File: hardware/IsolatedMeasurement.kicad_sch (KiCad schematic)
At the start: 25 parts, among them IC12 UCC12040DVE, IC15 ISO6763FDWR, IC2 MCP3561T-E_NC, IC5 SN74LVC1G07DBVR, IC6 AP7365-33YRG-13, IC9 REF193GSZ-REEL, J4 M300-MV10345M1

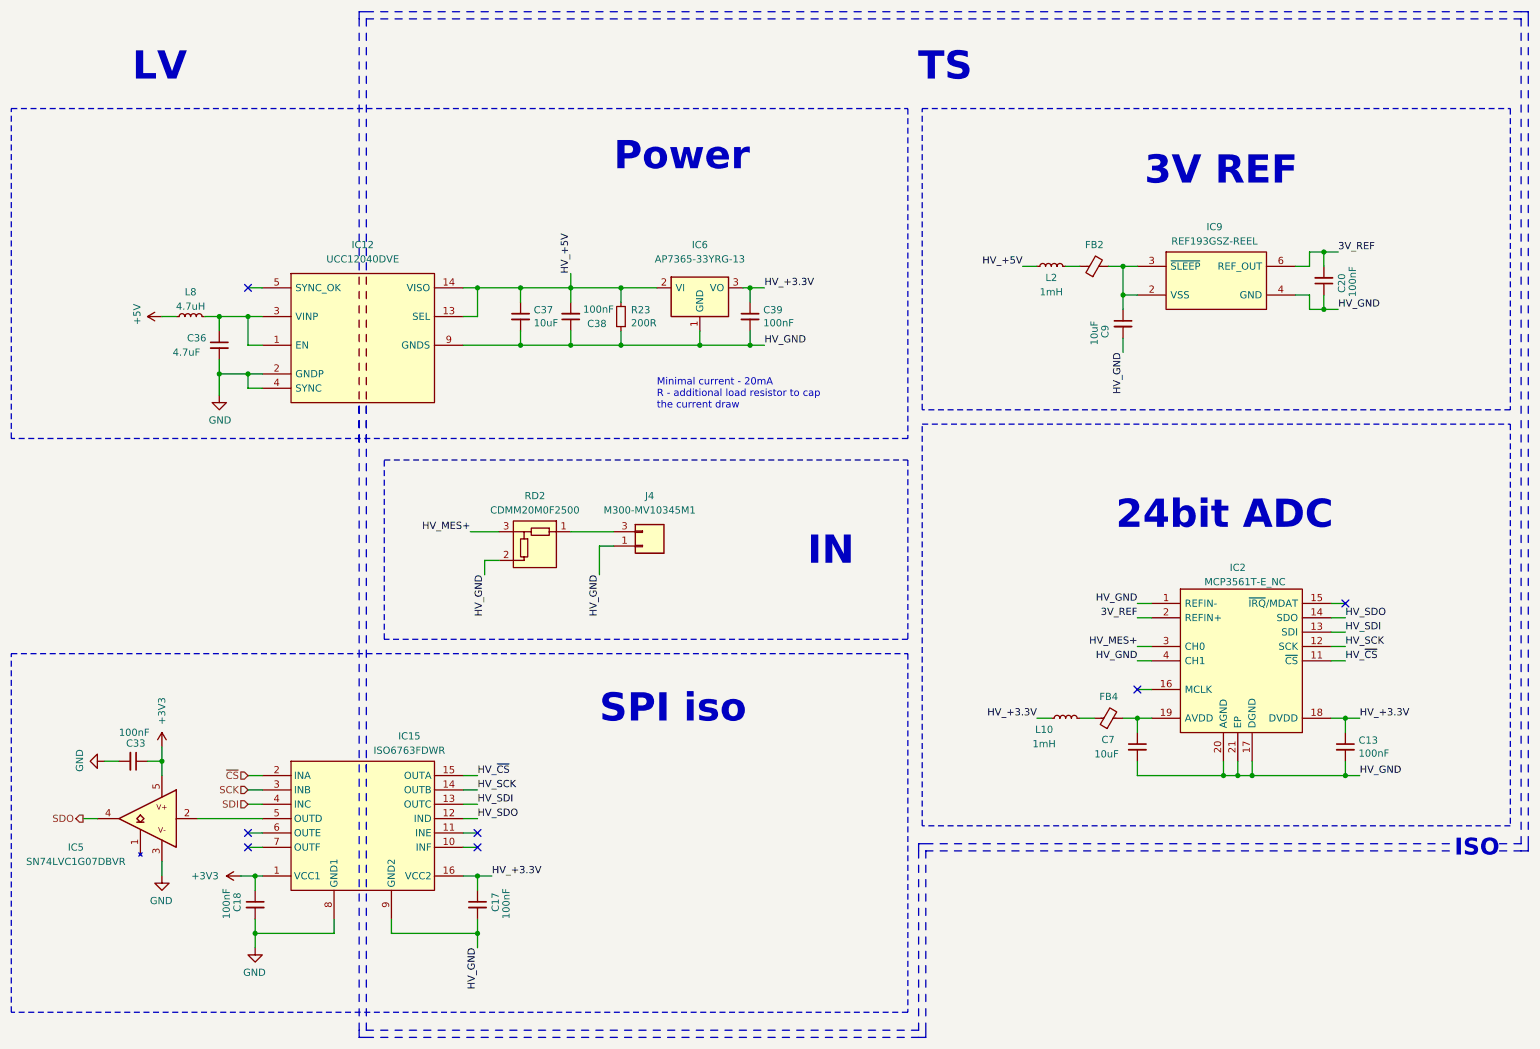
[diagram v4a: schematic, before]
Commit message: relay new driving logic, some ltc communication changes
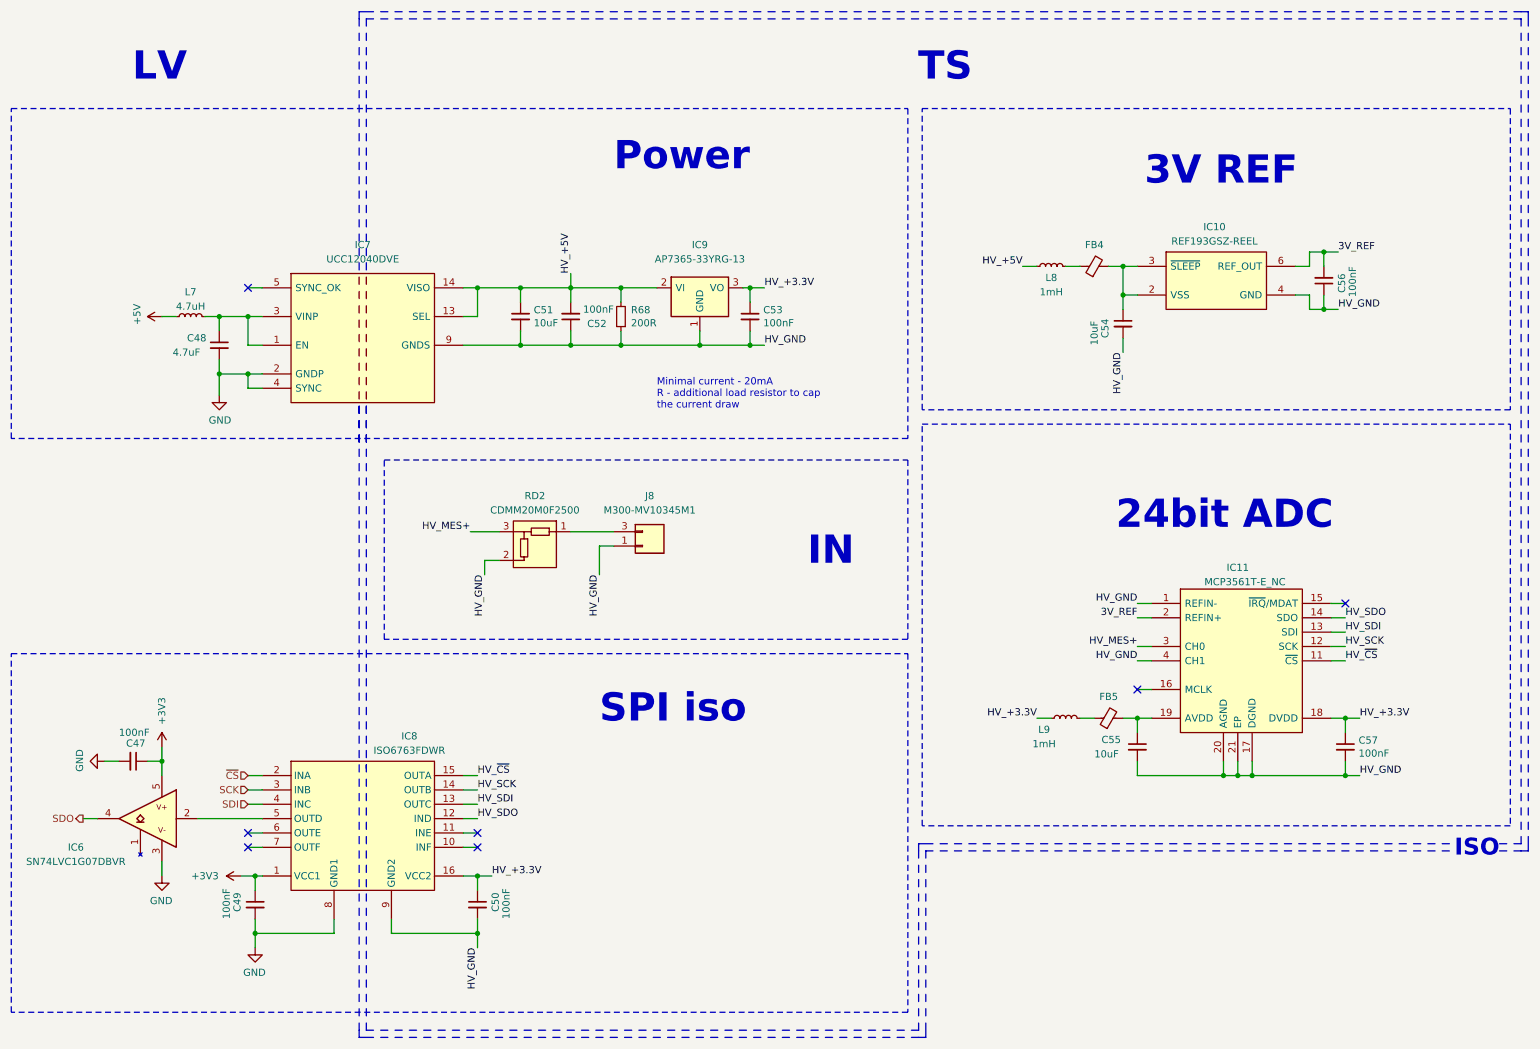
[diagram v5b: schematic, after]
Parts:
- renumbered C33 to C47, C36 to C48, C18 to C49, C17 to C50, C37 to C51, C38 to C52, C39 to C53, C9 to C54, C7 to C55, C20 to C56, C13 to C57, FB2 to FB4, FB4 to FB5, IC9 to IC10, IC2 to IC11, IC5 to IC6, IC12 to IC7, IC15 to IC8, IC6 to IC9, J4 to J8, L8 to L7, L2 to L8, L10 to L9, R23 to R68

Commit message: new hardware
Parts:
- IC7: footprint Samacsys:SOIC127P1030X265-16N -> Package_SO:SOIC-16W_7.5x10.3mm_P1.27mm
- IC8: footprint SOIC127P1030X265-16N -> Package_SO:SOIC-16W_7.5x10.3mm_P1.27mm
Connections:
- net HV_GND: now also J8.3; no longer J8.1
- net at RD2.1: now also J8.1; no longer J8.3

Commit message: major schematic changes
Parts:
- renumbered RD2 to RD1
